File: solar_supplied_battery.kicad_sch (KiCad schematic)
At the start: 12 parts, among them J1 Conn_01x02_Pin, J2 Conn_01x02_Pin, J3 Conn_01x02_Pin, J4 Conn_01x02_Pin, Q1 2N7002

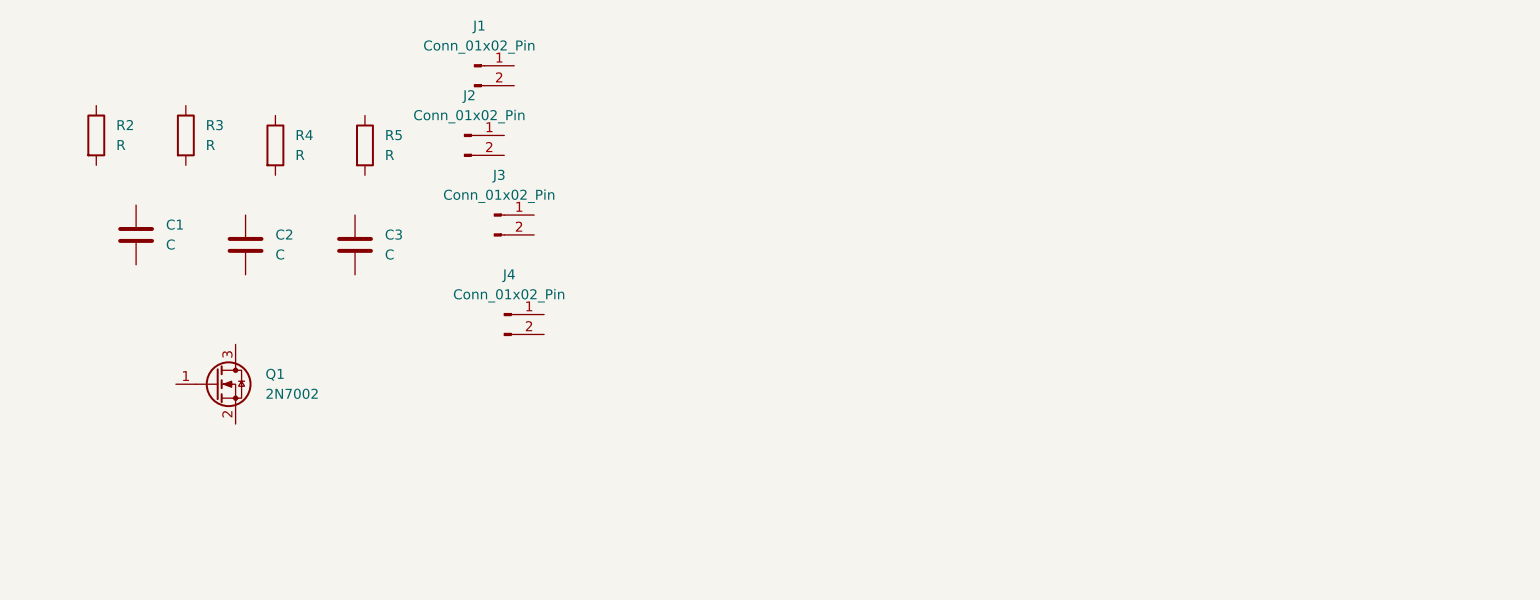
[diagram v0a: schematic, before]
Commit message: finished schema, just starting the pcb layout
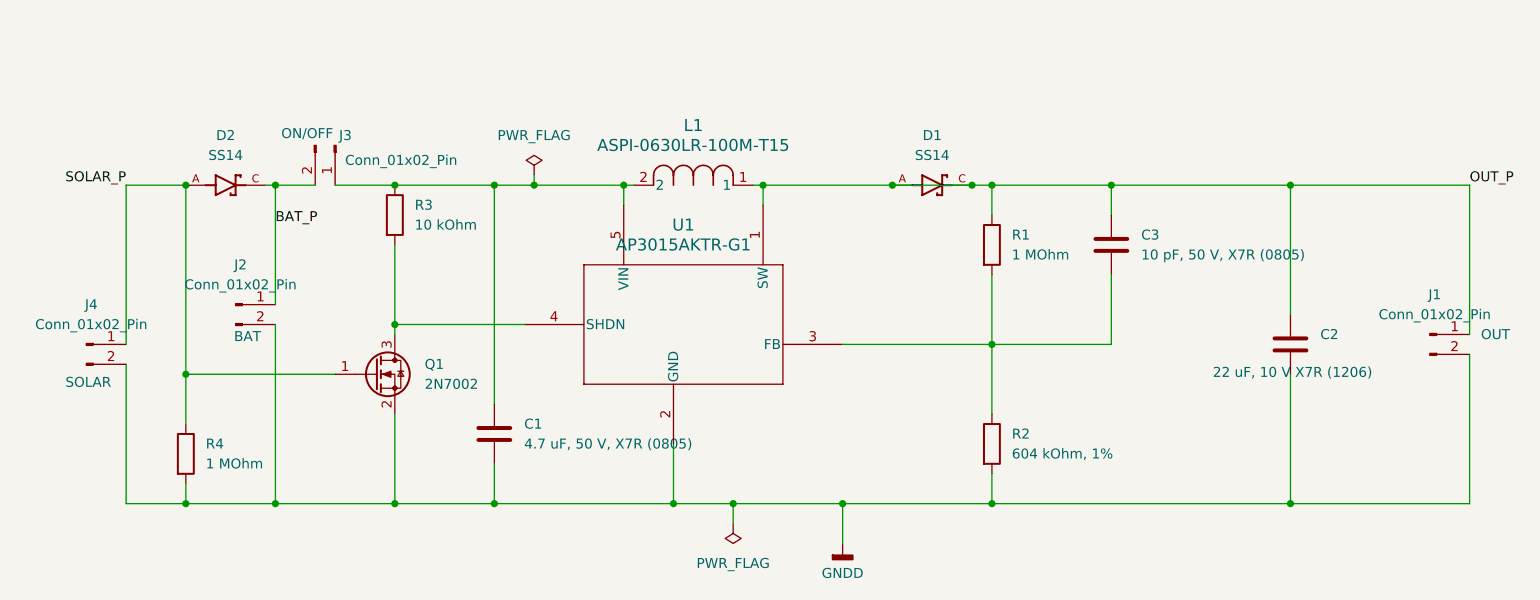
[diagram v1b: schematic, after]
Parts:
- added D1, D2: SS14, SS14:DIOM4325X250N, symbol SS14:SS14
- added L1: ASPI-0630LR-100M-T15, ul_ASPI-0630LR-100M-T15:IND_ASPI-0630LR_ABR, symbol Shottky:ASPI-0630LR-100M-T15
- added U1: AP3015AKTR-G1, ul_AP3015AKTR-G1:SOT23-5_1P55X2P9_DIO, symbol power_stepup:AP3015AKTR-G1
- C1: value C -> 4.7 uF, 50 V, X7R (0805); footprint (none) -> Capacitor_SMD:C_0805_2012Metric
- C2: value C -> 22 uF, 10 V X7R (1206); footprint (none) -> Capacitor_SMD:C_1206_3216Metric
- C3: value C -> 10 pF, 50 V, X7R (0805); footprint (none) -> Capacitor_SMD:C_0805_2012Metric
- J1: renamed from J2; footprint (none) -> Connector_PinHeader_2.54mm:PinHeader_1x02_P2.54mm_Vertical; Short description (none) -> OUT
- J2: renamed from J1; footprint (none) -> Connector_PinHeader_2.54mm:PinHeader_1x02_P2.54mm_Vertical; Short description (none) -> BAT
- J3: footprint (none) -> Connector_PinHeader_2.54mm:PinHeader_1x02_P2.54mm_Vertical; Short description (none) -> ON/OFF
- J4: footprint (none) -> Connector_PinHeader_2.54mm:PinHeader_1x02_P2.54mm_Horizontal; Short description (none) -> SOLAR
- R1: renamed from R2; value R -> 1 MOhm; footprint (none) -> Resistor_SMD:R_0805_2012Metric
- R2: renamed from R3; value R -> 604 kOhm, 1%; footprint (none) -> Resistor_SMD:R_0805_2012Metric
- R3: renamed from R4; value R -> 10 kOhm; footprint (none) -> Resistor_SMD:R_0805_2012Metric
- R4: renamed from R5; value R -> 1 MOhm; footprint (none) -> Resistor_SMD:R_0805_2012Metric
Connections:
- net at R2.1: now also C3.2, R1.2, U1.3 (FB)
- net GNDD: now reaches R2.2
- net GNDD: now also C1.2, C2.2, J1.2 (Pin_2), J2.2 (Pin_2), J4.2 (Pin_2), Q1.2 (S), R4.2, U1.2 (GND)
- net at C1.1: now also J3.1 (Pin_1), R3.1, L1.2, U1.5 (VIN)
- net BAT_P: now reaches J2.1 (Pin_1)
- net BAT_P: now also J3.2 (Pin_2), D2.C
- net SOLAR_P: now reaches R4.1
- net SOLAR_P: now also J4.1 (Pin_1), Q1.1 (G), D2.A
- net OUT_P: now reaches C2.1
- net OUT_P: now also C3.1, J1.1 (Pin_1), R1.1, D1.A, D1.C, L1.1, U1.1 (SW)
- net at R3.2: now also Q1.3 (D), U1.4 (SHDN)
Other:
- moved on the sheet: C1, C2, C3, J1, J2, J3, J4, Q1, R1, R2, R3, R4

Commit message: starting routes
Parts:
- J1, J2: footprint Connector_PinHeader_2.54mm:PinHeader_1x02_P2.54mm_Vertical -> TerminalBlock:TerminalBlock_MaiXu_MX126-5.0-02P_1x02_P5.00mm
- J4: footprint Connector_PinHeader_2.54mm:PinHeader_1x02_P2.54mm_Horizontal -> TerminalBlock:TerminalBlock_MaiXu_MX126-5.0-02P_1x02_P5.00mm
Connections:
- net OUT_P: no longer D1.A, L1.1, U1.1 (SW)
- new net: D1.A, L1.1, U1.1 (SW)
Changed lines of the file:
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@@
-	)
-	(junction
-		(at 176.53 91.44)
-		(diameter 0)
-		(color 0 0 0 0)
-	)
-	(junction
-		(at 166.37 91.44)
-		(diameter 0)
-		(color 0 0 0 0)
 	)
 	(junction
@@
 		(pts
 			(xy 115.57 91.44) (xy 115.57 119.38)
-		)
-		(stroke
-			(width 0)
-			(type default)
-		)
-	)
-	(wire
-		(pts
-			(xy 166.37 91.44) (xy 176.53 91.44)
 		)
 		(stroke
@@
 			)
 		)
-		(property "Footprint" "Connector_PinHeader_2.54mm:PinHeader_1x02_P2.54mm_Vertical"
+		(property "Footprint" "TerminalBlock:TerminalBlock_MaiXu_MX126-5.0-02P_1x02_P5.00mm"
 			(at 82.55 106.68 0)
 			(hide yes)
@@
 			)
 		)
-		(property "Footprint" "Connector_PinHeader_2.54mm:PinHeader_1x02_P2.54mm_Vertical"
+		(property "Footprint" "TerminalBlock:TerminalBlock_MaiXu_MX126-5.0-02P_1x02_P5.00mm"
 			(at 234.95 110.49 0)
 			(hide yes)
@@
 			)
 		)
-		(property "Footprint" "Connector_PinHeader_2.54mm:PinHeader_1x02_P2.54mm_Horizontal"
+		(property "Footprint" "TerminalBlock:TerminalBlock_MaiXu_MX126-5.0-02P_1x02_P5.00mm"
 			(at 63.5 111.76 0)
 			(hide yes)

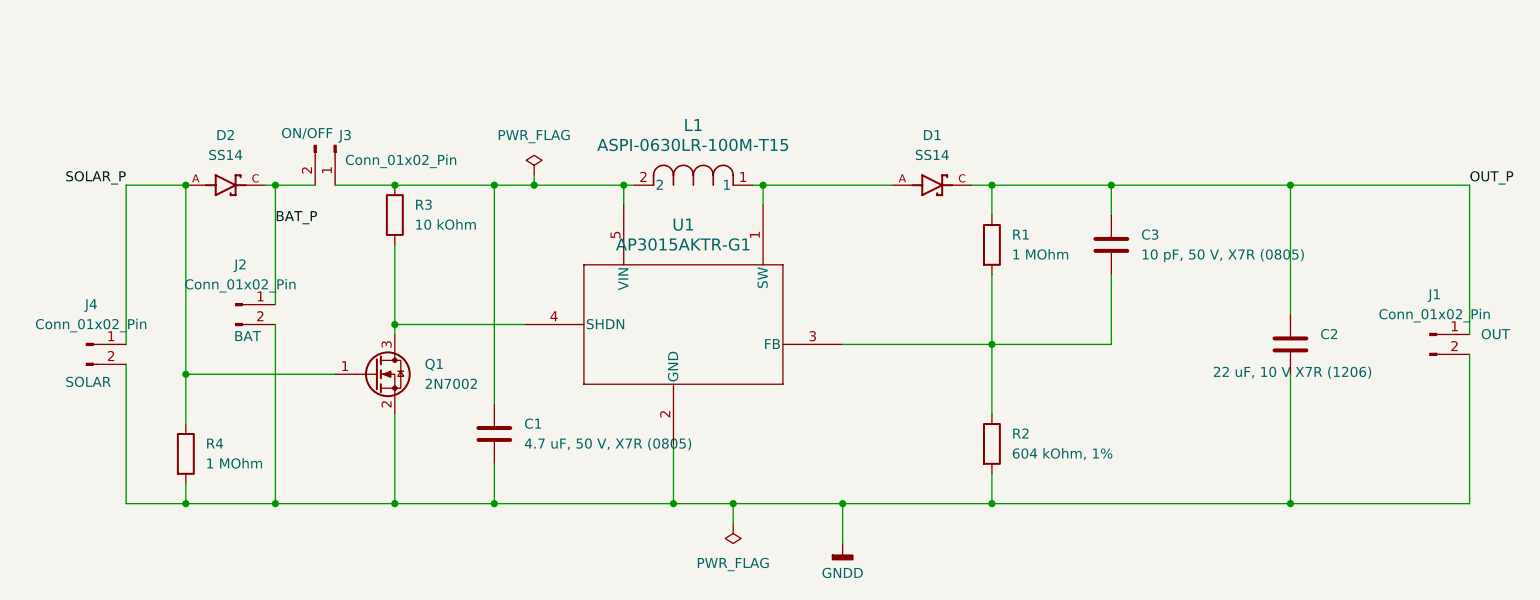
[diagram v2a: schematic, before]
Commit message: reorganized folders and importing footprints
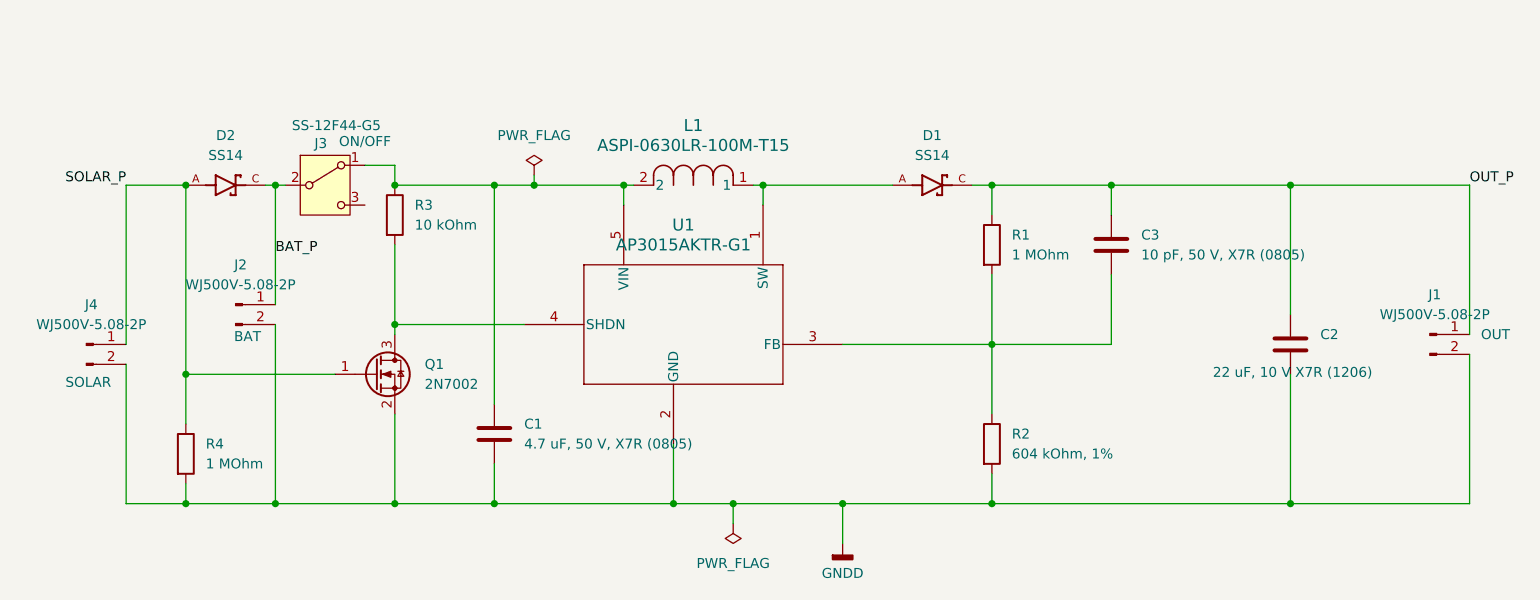
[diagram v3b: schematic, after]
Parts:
- J1, J2, J4: value Conn_01x02_Pin -> WJ500V-5.08-2P; footprint TerminalBlock:TerminalBlock_MaiXu_MX126-5.0-02P_1x02_P5.00mm -> TerminalBlock_Phoenix:TerminalBlock_Phoenix_MKDS-3-2-5.08_1x02_P5.08mm_Horizontal; JLCPCB Part (none) -> C8465
- J3: value Conn_01x02_Pin -> SS-12F44-G5; footprint Connector_PinHeader_2.54mm:PinHeader_1x02_P2.54mm_Vertical -> TerminalBlock_Phoenix:TerminalBlock_Phoenix_MKDS-3-2-5.08_1x02_P5.08mm_Horizontal; symbol Connector:Conn_01x02_Pin -> Switch:SW_SPDT; JLCPCB Part (none) -> C136718

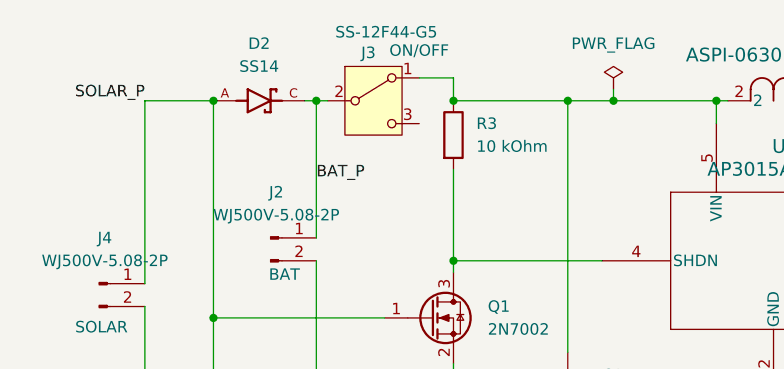
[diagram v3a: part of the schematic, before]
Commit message: finished routing, now just have to make vias for the ground fills
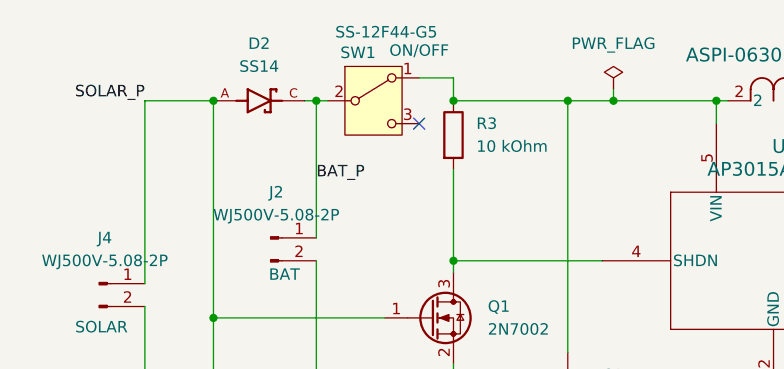
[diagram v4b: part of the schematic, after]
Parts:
- SW1: renamed from J3; footprint TerminalBlock_Phoenix:TerminalBlock_Phoenix_MKDS-3-2-5.08_1x02_P5.08mm_Horizontal -> jlcpcb:SW-TH_SS-12F44-G5
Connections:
- no-connect marks 0 -> 1
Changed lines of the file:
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@@
 		(color 0 0 0 0)
+	)
+	(no_connect
+		(at 99.06 93.98)
 	)
 	(wire
@@
 		(in_pos_files yes)
 		(dnp no)
-		(property "Reference" "J3"
+		(property "Reference" "SW1"
 			(at 94.234 86.106 0)
 			(show_name no)
@@
 			)
 		)
-		(property "Footprint" "TerminalBlock_Phoenix:TerminalBlock_Phoenix_MKDS-3-2-5.08_1x02_P5.08mm_Horizontal"
+		(property "Footprint" "jlcpcb:SW-TH_SS-12F44-G5"
 			(at 93.98 91.44 0)
 			(hide yes)
@@
 			(project "solar_supplied_battery"
 				(path "/2c9a11ac-7ab7-4264-a62c-d36ea767d92d"
-					(reference "J3")
+					(reference "SW1")
 					(unit 1)
 				)

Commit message: finalized the physical components, just have to do gerber and bom
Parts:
- C1: value 4.7 uF, 50 V, X7R (0805) -> 4.7 µF, 25 V, X5R (0805); JLCPCB Part (none) -> C1779
- C2: value 22 uF, 10 V X7R (1206) -> 22 µF, 25 V, X5R (1206); JLCPCB Part (none) -> C12891
- C3: value 10 pF, 50 V, X7R (0805) -> 10 pF, 50 V, C0G (0805); JLCPCB Part (none) -> C157608
- D1, D2: footprint SS14:DIOM4325X250N -> SS14:SS14; JLCPCB Part (none) -> C2480
- L1: footprint ul_ASPI-0630LR-100M-T15:IND_ASPI-0630LR_ABR -> ASPI-0630LR-100M-T15:IND_ASPI-0630LR-100M-T15; JLCPCB Part (none) -> C1334133
- Q1: JLCPCB Part (none) -> C8545
- R1, R4: JLCPCB Part (none) -> C17514
- R2: JLCPCB Part (none) -> C17776
- R3: JLCPCB Part (none) -> C17414
- SW1: footprint jlcpcb:SW-TH_SS-12F44-G5 -> SW-TH_SS-12F44-G5:SW-TH_SS-12F44-G5
- U1: footprint ul_AP3015AKTR-G1:SOT23-5_1P55X2P9_DIO -> AP3015AKTR-G1:AP3015AKTR-G1; JLCPCB Part (none) -> C154879
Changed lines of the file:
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@@
 			)
 		)
-		(property "JLCPCB Part" ""
+		(property "JLCPCB Part" "C17776"
 			(at 179.07 124.46 0)
 			(hide yes)
@@
 			)
 		)
-		(property "Value" "4.7 uF, 50 V, X7R (0805)"
+		(property "Value" "4.7 µF, 25 V, X5R (0805)"
 			(at 119.38 124.4599 0)
 			(show_name no)
@@
 			)
 		)
-		(property "JLCPCB Part" ""
+		(property "JLCPCB Part" "C1779"
 			(at 115.57 123.19 0)
 			(hide yes)
@@
 			)
 		)
-		(property "Footprint" "SS14:DIOM4325X250N"
+		(property "Footprint" "SS14:SS14"
 			(at 171.45 91.44 0)
 			(hide yes)
@@
 			)
 		)
-		(property "JLCPCB Part" ""
+		(property "JLCPCB Part" "C2480"
 			(at 171.45 91.44 0)
 			(hide yes)
@@
 			)
 		)
-		(property "JLCPCB Part" ""
+		(property "JLCPCB Part" " C17514"
 			(at 76.2 125.73 0)
 			(hide yes)
@@
 			)
 		)
-		(property "Value" "22 uF, 10 V X7R (1206)"
+		(property "Value" "22 µF, 25 V, X5R (1206)"
 			(at 207.264 115.316 0)
 			(show_name no)
@@
 			)
 		)
-		(property "JLCPCB Part" ""
+		(property "JLCPCB Part" " C12891"
 			(at 217.17 111.76 0)
 			(hide yes)
@@
 			)
 		)
-		(property "Value" "10 pF, 50 V, X7R (0805)"
+		(property "Value" "10 pF, 50 V, C0G (0805)"
 			(at 198.12 100.3299 0)
 			(show_name no)
@@
 			)
 		)
-		(property "JLCPCB Part" ""
+		(property "JLCPCB Part" "C157608"
 			(at 194.31 99.06 0)
 			(hide yes)
@@
 			)
 		)
-		(property "Footprint" "ul_ASPI-0630LR-100M-T15:IND_ASPI-0630LR_ABR"
+		(property "Footprint" "ASPI-0630LR-100M-T15:IND_ASPI-0630LR-100M-T15"
 			(at 133.35 91.44 0)
 			(hide yes)
@@
 			)
 		)
-		(property "JLCPCB Part" ""
+		(property "JLCPCB Part" "C1334133"
 			(at 133.35 91.44 0)
 			(hide yes)
+			(show_name no)
+			(do_not_autoplace no)
+			(effects
+				(font
+					(size 1.27 1.27)
+				)
+			)
+		)
+		(property "Short description" ""
+			(at 133.35 91.44 0)
+			(show_name no)
+			(do_not_autoplace no)
+			(effects
+				(font
+					(size 1.27 1.27)
+				)
+			)
+		)
+		(property "Purpose" ""
+			(at 133.35 91.44 0)
 			(show_name no)
 			(do_not_autoplace no)
@@
 			)
 		)
-		(property "JLCPCB Part" ""
+		(property "JLCPCB Part" "C17414"
 			(at 102.87 95.25 0)
 			(hide yes)
@@
 			)
 		)
-		(property "JLCPCB Part" ""
+		(property "JLCPCB Part" "C8545"
 			(at 100.33 115.57 0)
 			(hide yes)
@@
 			)
 		)
-		(property "Footprint" "jlcpcb:SW-TH_SS-12F44-G5"
+		(property "Footprint" "SW-TH_SS-12F44-G5:SW-TH_SS-12F44-G5"
 			(at 93.98 91.44 0)
 			(hide yes)
@@
 			)
 		)
-		(property "Footprint" "ul_AP3015AKTR-G1:SOT23-5_1P55X2P9_DIO"
+		(property "Footprint" "AP3015AKTR-G1:AP3015AKTR-G1"
 			(at 119.38 106.68 0)
 			(hide yes)
@@
 			)
 		)
-		(property "JLCPCB Part" ""
+		(property "JLCPCB Part" "C154879"
 			(at 119.38 106.68 0)
 			(hide yes)
@@
 			)
 		)
-		(property "JLCPCB Part" ""
+		(property "JLCPCB Part" " C17514"
 			(at 179.07 99.06 0)
 			(hide yes)
@@
 			)
 		)
-		(property "Footprint" "SS14:DIOM4325X250N"
+		(property "Footprint" "SS14:SS14"
 			(at 81.28 91.44 0)
 			(hide yes)
@@
 			)
 		)
-		(property "JLCPCB Part" ""
+		(property "JLCPCB Part" "C2480"
 			(at 81.28 91.44 0)
 			(hide yes)

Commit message: finished layout and bom
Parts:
- C2: JLCPCB Part C12891 -> C12891
- R4: JLCPCB Part C17514 -> C17514
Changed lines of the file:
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@@
 			)
 		)
-		(property "JLCPCB Part" " C17514"
+		(property "JLCPCB Part" "C17514"
 			(at 76.2 125.73 0)
 			(hide yes)
@@
 			)
 		)
-		(property "JLCPCB Part" " C12891"
+		(property "JLCPCB Part" "C12891"
 			(at 217.17 111.76 0)
 			(hide yes)
